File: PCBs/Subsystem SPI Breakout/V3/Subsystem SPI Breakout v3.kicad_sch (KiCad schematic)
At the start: 11 parts, among them Q1 BS170, Q5 NPN transistor

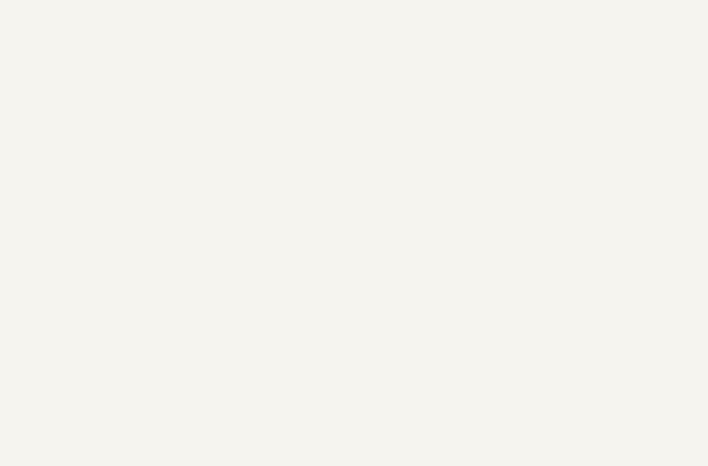
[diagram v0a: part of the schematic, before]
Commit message: Started Work on SPI Board Rework
need to change the size of the board for the 2.8" screen and also change the connector out, as well as use the raw parts for the bi-directional logic level converter.
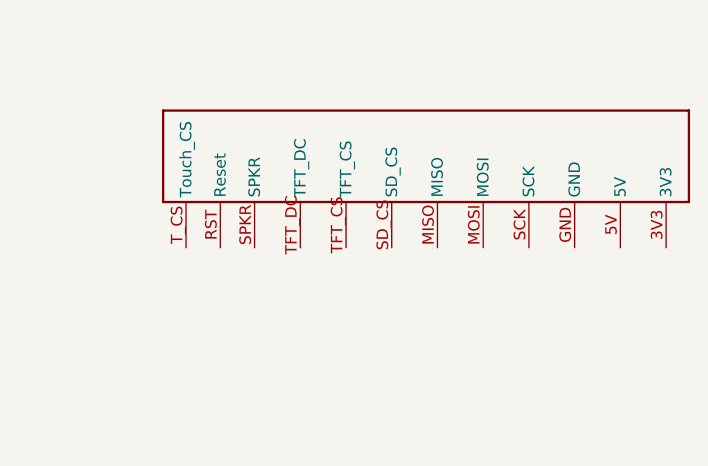
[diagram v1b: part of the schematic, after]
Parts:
- added C1: ~, Subsystem Main Extra Symbols:SPI_HEADER_RIBBON_CONNECTOR_V2, symbol Subsystem Extra Symbols:SPI_HEADER_WITH_RESET
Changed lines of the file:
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@@
+	)
+	(symbol
+		(lib_id "Subsystem Extra Symbols:SPI_HEADER_WITH_RESET")
+		(at 214.63 31.75 180)
+		(unit 1)
+		(exclude_from_sim no)
+		(in_bom yes)
+		(on_board yes)
+		(dnp no)
+		(fields_autoplaced yes)
+		(property "Reference" "C1"
+			(at 219.71 31.75 0)
+			(effects
+				(font
+					(size 1.27 1.27)
+				)
+				(hide yes)
+			)
+		)
+		(property "Value" "~"
+			(at 219.71 31.75 0)
+			(effects
+				(font
+					(size 1.27 1.27)
+				)
+				(hide yes)
+			)
+		)
+		(property "Footprint" "Subsystem Main Extra Symbols:SPI_HEADER_RIBBON_CONNECTOR_V2"
+			(at 214.884 25.146 0)
+			(effects
+				(font
+					(size 1.27 1.27)
+				)
+				(hide yes)
+			)
+		)
+		(property "Datasheet" ""
+			(at 219.71 31.75 0)
+			(effects
+				(font
+					(size 1.27 1.27)
+				)
+				(hide yes)
+			)
+		)
+		(property "Description" ""
+			(at 219.71 31.75 0)
+			(effects
+				(font
+					(size 1.27 1.27)
+				)
+				(hide yes)
+			)
+		)
+		(pin "GND"
+		)
+		(pin "SPKR"
+		)
+		(pin "3V3"
+		)
+		(pin "TFT_CS"
+		)
+		(pin "T_CS"
+		)
+		(pin "MOSI"
+		)
+		(pin "SCK"
+		)
+		(pin "MISO"
+		)
+		(pin "SD_CS"
+		)
+		(pin "TFT_DC"
+		)
+		(pin "5V"
+		)
+		(pin "RST"
+		)
+		(instances
+			(project ""
+				(path "/febd836d-dda2-47e2-b3cf-62a76efd61a3"
+					(reference "C1")
+					(unit 1)
+				)
+			)
+		)
 	)
 	(symbol

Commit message: Updates to V3 of the SPI Breakout Board
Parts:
- removed 1: ~, Subsystem Main:SPI_HEADER_RIBBON_CONNECTOR, symbol Subsystem Main:SPI_HEADERSPI_HEADER_RIBBON_CONNECTOR
- added Q2, Q3, Q4, Q6, Q7, Q8, Q9: BS170, Package_TO_SOT_THT:TO-92_Inline, symbol Transistor_FET:BS170
- added R10, R11, R12, R13, R14, R15, R16, R17, R18, R19, R3, R4, R5, R6: 10k Ω, Subsystem Main:THROUGH_HOLE_RESISTOR, symbol Subsystem Main:THROUGH_HOLE_RESISTOR
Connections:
- net 3V3: now also C1.3V3, Q2.2 (G), Q3.2 (G), Q4.2 (G), Q6.2 (G), Q7.2 (G), Q8.2 (G), Q9.2 (G), R10.P$1, R12.P$1, R14.P$1, R16.P$1, R18.P$1, R3.P$1, R5.P$1
- net 5V: now also C1.5V, R11.P$1, R13.P$1, R15.P$1, R19.P$1, R4.P$1, R6.P$1
- net GND: now also C1.GND
- net SCK_3V3: now reaches Q1.1 (D), R1.P$2
- net SCK_3V3: now also U2.SCK, U2.SD_SCK, U2.T_CLK
- net at R8.P$2: now also C1.SPKR
- net MOSI_3V3: now reaches U2.SDI(MOSI), U2.SD_MOSI
- net MOSI_3V3: now also U2.T_DIN, Q2.1 (D), R3.P$2
- net CS_TOUCH_3V3: now reaches U2.T_CS
- net CS_TOUCH_3V3: now also Q8.1 (D), R16.P$2
- net MISO_3V3: now reaches U2.T_DO
- net MISO_3V3: now also Q3.1 (D), R5.P$2
- net MISO_5V: now reaches C1.MISO
- net MISO_5V: now also Q3.3 (S), R6.P$2
- net MOSI_5V: now reaches C1.MOSI
- net MOSI_5V: now also Q2.3 (S), R4.P$2
- net RESET_5V: now reaches C1.RST (Reset)
- net RESET_5V: now also Q9.3 (S), R19.P$2
- net SCK_5V: now reaches C1.SCK
- net SCK_5V: now also Q1.3 (S), R2.P$2
- net CS_SD_5V: now reaches C1.SD_CS
- net CS_SD_5V: now also Q7.3 (S), R15.P$2
- net CS_TFT_5V: now reaches C1.TFT_CS
- net CS_TFT_5V: now also Q4.3 (S), R11.P$2
- net DC_5V: now reaches C1.TFT_DC
- net DC_5V: now also Q6.3 (S), R13.P$2
- net CS_TOUCH_5V: now reaches C1.T_CS (Touch_CS)
- net CS_TOUCH_5V: now also Q8.3 (S), R17.P$2
- new net CS_SD_3V3: Q7.1 (D), R14.P$2
- new net CS_TFT_3V3: Q4.1 (D), R10.P$2
- new net DC_3V3: Q6.1 (D), R12.P$2
- new net RESET_3V3: Q9.1 (D), R18.P$2
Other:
- moved on the sheet: LS1, Q1, Q5, U2, U3

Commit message: Finished SPI Breakout Board V3
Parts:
- added U1: ~, Subsystem Main Extra Symbols:T_IRQ, symbol Subsystem Extra Symbols:T_irq
- Amplifying Transistor1: renamed from Q5
- U2: footprint Subsystem Main:2.4'_TFT_SPI_ILI9341_WITH_SD_CARD -> Subsystem Main:2.8__TFT_SPI_ILI9341_WITH_SD_CARD
- renumbered Q7 to CS_SD1, Q4 to CS_TFT1, Q8 to CS_Touch1, Q6 to DC1, Q3 to MISO1, Q2 to MOSI1, Q9 to RESET1, Q1 to SCK1
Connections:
- net 5V: now also R17.P$1
- net CS_SD_3V3: now also U2.SD_CS
- net CS_TFT_3V3: now also U2.CS
- net DC_3V3: now also U2.DC
- net MISO_3V3: now also U2.SDO(MISO), U2.SD_MISO
- net RESET_3V3: now also U2.RESET
- net at U2.T_IRQ: now also U1.1 (T_IRQ)

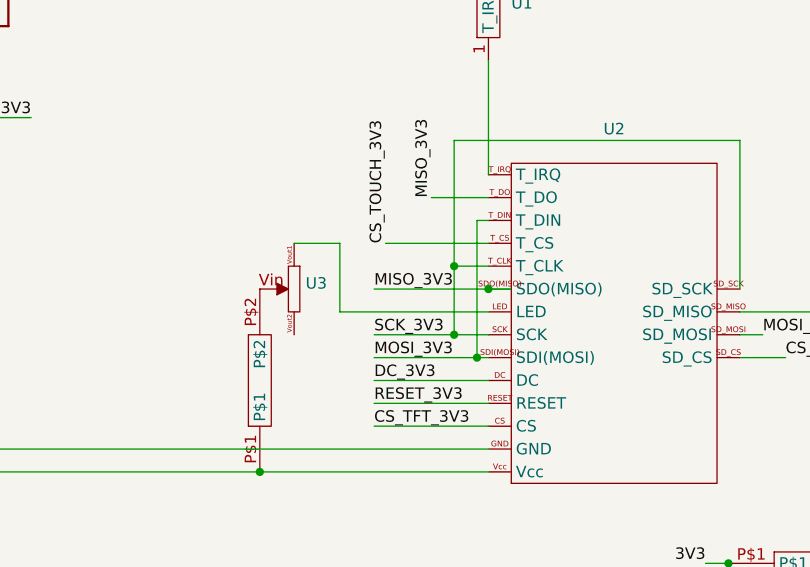
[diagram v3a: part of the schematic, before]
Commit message: Fixed some labels on the silkscreen
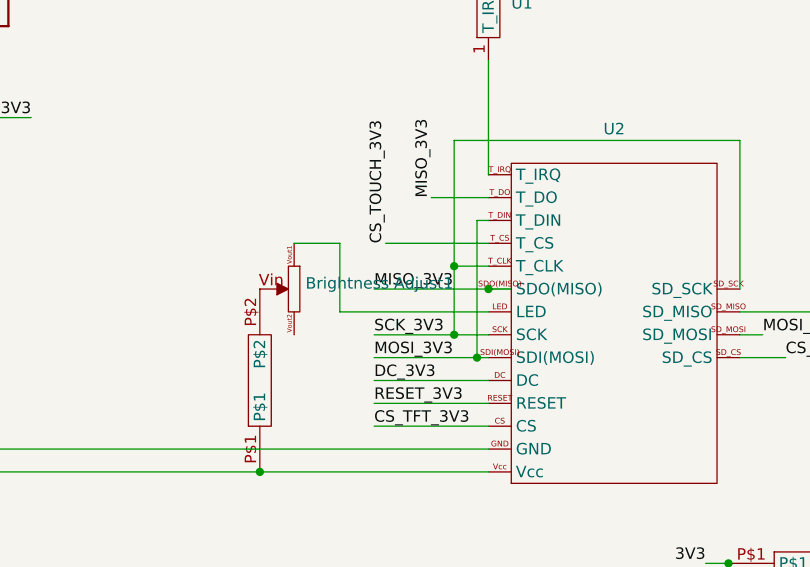
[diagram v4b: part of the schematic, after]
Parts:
- Brightness Adjust1: renamed from U3
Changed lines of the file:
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@@
 		(dnp no)
 		(fields_autoplaced yes)
-		(property "Reference" "U3"
+		(property "Reference" "Brightness Adjust1"
 			(at 105.41 52.7049 90)
 			(effects
@@
 			(project ""
 				(path "/febd836d-dda2-47e2-b3cf-62a76efd61a3"
-					(reference "U3")
+					(reference "Brightness Adjust1")
 					(unit 1)
 				)
